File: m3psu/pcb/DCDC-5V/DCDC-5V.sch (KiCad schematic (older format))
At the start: 18 parts, among them J1 WEST TOP, J2 WEST BOT, J3 NORTH TOP, J4 EAST TOP, J5 EAST BOT, J6 NORTH BOT

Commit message: Work on DCDC-5V schematic and board
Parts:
- removed C?: 100n, symbol C
- added C1, C10, C6: 100n, agg:0402, symbol C
- added C11, C7: 3n3, agg:0402, symbol C
- added C12, C8, C9: 22µ, agg:0805, symbol C
- added C5: 10µ, agg:0805, symbol C
- added IC2: TPS62133, agg:QFN-16-EP-TI, symbol TPS62133
- added IC3: TPS62152, agg:QFN-16-EP-TI, symbol TPS62152
- added L1: 2µ2, agg:TYS5040, symbol L
- added L2: 3µ3, agg:VLS201610HBX-1, symbol L
- added Q1, Q2, Q3, Q4: NFET_GDS, agg:SOT-883-B, symbol NFET_GDS
- added Q5, Q6, Q7, Q8: PFET_GDS, agg:SON2x2, symbol PFET_GDS
- added R10, R11, R12, R13, R14, R15, R16, R9: 33k, agg:0402, symbol R
- added R17, R18, R19, R20: 10m, agg:0603, symbol R
- C2, C3, C4: renamed from C?; footprint (none) -> agg:0402
- R2, R3, R4, R5, R6, R7, R8: renamed from R?; footprint (none) -> agg:0402
- gave numbers to parts that had none: 1
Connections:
- net 3v3: now also IC1.10 (VPWR), C1.2, C12.1, IC3.14 (VOS), IC3.7 (FSW), L2.2
- net 5v_CAM: now also IC1.44 (I_SENSE_1-), R18.1
- net 5v_CAN: now also IC1.42 (I_SENSE_0-), R17.1
- net 5v_IMU: now also IC1.46 (I_SENSE_2-), R19.1
- net 5v_RADIO: now also IC1.48 (I_SENSE_3-), R20.1
- net GND: now also C1.1, C10.2, C11.2, C12.2, C5.2, C6.2, C7.2, C8.2, C9.2, IC2.15 (PGND), IC2.16 (PGND), IC2.5 (FB), IC2.6 (AGND), IC2.7 (FSW), IC2.8 (DEF), IC2.EP, IC3.15 (PGND), IC3.16 (PGND), IC3.5 (FB), IC3.6 (AGND), IC3.8 (DEF), IC3.EP, Q1.S, Q2.S, Q3.S, Q4.S
- net VCC: now also C10.1, C5.1, C6.1, C9.1, IC2.10 (AVIN), IC2.11 (PVIN), IC2.12 (PVIN), IC2.13 (EN), IC3.10 (AVIN), IC3.11 (PVIN), IC3.12 (PVIN), IC3.13 (EN)
- net ISNS0+: now reaches IC1.1 (V_SENSE_0+)
- net ISNS0+: now also IC1.41 (I_SENSE_0+), Q5.D, R17.2
- net VEN_0: now reaches IC1.3 (VOUT_EN0)
- net VEN_0: now also Q1.G, R9.2
- net VEN_1: now reaches IC1.4 (VOUT_EN1)
- net VEN_1: now also Q2.G, R10.2
- net ISNS1+: now reaches IC1.43 (I_SENSE_1+)
- net ISNS1+: now also IC1.63 (V_SENSE_1+), Q6.D, R18.2
- net ISNS2+: now reaches IC1.45 (I_SENSE_2+)
- net ISNS2+: now also IC1.61 (V_SENSE_2+), Q7.D, R19.2
- net ISNS3+: now reaches IC1.47 (I_SENSE_3+)
- net ISNS3+: now also IC1.49 (V_SENSE_3+), Q8.D, R20.2
- net VEN_2: now reaches IC1.5 (VOUT_EN2)
- net VEN_2: now also Q3.G, R11.2
- net V_DIST: now reaches IC1.55 (IIN_SENSE+)
- net V_DIST: now also IC1.56 (IIN_SENSE-), IC1.9 (VIN_SENSE), C8.1, IC2.14 (VOS), L1.2, Q5.S, Q6.S, Q7.S, Q8.S, R10.1, R11.1, R12.1, R13.1, R14.1, R15.1, R16.1, R9.1
- net VEN_3: now reaches IC1.6 (VOUT_EN3)
- net VEN_3: now also Q4.G, R12.2
- new net: IC2.1 (SW), IC2.2 (SW), IC2.3 (SW), L1.1
- new net: C7.1, IC2.9 (SS/TR)
- new net: IC3.1 (SW), IC3.2 (SW), IC3.3 (SW), L2.1
- new net: C11.1, IC3.9 (SS/TR)
- new net: Q1.D, Q5.G, R13.2
- new net: Q2.D, Q6.G, R14.2
- new net: Q3.D, Q7.G, R15.2
- new net: Q4.D, Q8.G, R16.2
- no-connect marks 13 -> 15
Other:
- note added: "3.3V 1A fixed output"
- note added: "5V 3A fixed output"
- note added: "CHANNEL 0"
- note added: "CHANNEL 1"
- note added: "CHANNEL 2"
- note added: "CHANNEL 3"
- moved on the sheet: C2

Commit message: Add note about temporary footprint
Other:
- note added: "WRONG FOOTPRINT\nTEMPORARILY"
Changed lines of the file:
@@
 Wire Wire Line
 	9800 4000 9800 3950
+Text Notes 2400 1100 0    60   ~ 0
+WRONG FOOTPRINT\nTEMPORARILY
 $EndSCHEMATC

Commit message: Finish DCDC-5V schematic, first go at routing
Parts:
- added R1: 5k49, agg:0402, symbol R
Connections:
- net 3v3: now also R1.1
- net GND: now also IC1.15 (TSENSE_0), IC1.16 (TSENSE_1), IC1.27 (TSENSE_2), IC1.34 (TSENSE_3)
- net PSU_RSVD: now reaches J3.5
- net PSU_RSVD: now also J6.5
- net at IC1.18 (SHARE_CLK): now also R1.2
- no-connect marks 15 -> 8

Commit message: Update with correct inductor footprint
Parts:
- L1: footprint agg:TYS5040 -> agg:XFL4020
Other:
- note removed: "WRONG FOOTPRINT\nTEMPORARILY"
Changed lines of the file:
@@
 F 0 "L1" H 2500 1250 50  0000 C CNN
 F 1 "2µ2" H 2500 1150 50  0000 C CNN
-F 2 "agg:TYS5040" H 2450 1200 50  0001 C CNN
+F 2 "agg:XFL4020" H 2450 1200 50  0001 C CNN
 F 3 "" H 2450 1200 50  0001 C CNN
 F 4 "2289216" H 2450 1200 60  0001 C CNN "Farnell"
@@
 	1    0    0    -1
 $EndComp
-Text Notes 2400 1100 0    60   ~ 0
-WRONG FOOTPRINT\nTEMPORARILY
 Text Label 10100 3500 2    60   ~ 0
 PSU_RSVD
@@
 	8750 700  8750 750
 $Comp
-L GND #PWR?
+L GND #PWR054
 U 1 1 58B616BB
 P 5300 4950
-F 0 "#PWR?" H 5170 4990 50  0001 L CNN
+F 0 "#PWR054" H 5170 4990 50  0001 L CNN
 F 1 "GND" H 5300 4850 50  0000 C CNN
 F 2 "" H 5300 4950 60  0001 C CNN
@@
 	5300 4950 5250 4950
 $Comp
-L GND #PWR?
+L GND #PWR055
 U 1 1 58B61DC1
 P 5300 4150
-F 0 "#PWR?" H 5170 4190 50  0001 L CNN
+F 0 "#PWR055" H 5170 4190 50  0001 L CNN
 F 1 "GND" H 5300 4050 50  0000 C CNN
 F 2 "" H 5300 4150 60  0001 C CNN
@@
 	5300 4150 5250 4150
 $Comp
-L GND #PWR?
+L GND #PWR056
 U 1 1 58B62495
 P 5300 3350
-F 0 "#PWR?" H 5170 3390 50  0001 L CNN
+F 0 "#PWR056" H 5170 3390 50  0001 L CNN
 F 1 "GND" H 5300 3250 50  0000 C CNN
 F 2 "" H 5300 3350 60  0001 C CNN
@@
 	5300 3350 5250 3350
 $Comp
-L GND #PWR?
+L GND #PWR057
 U 1 1 58B62E35
 P 5300 2550
-F 0 "#PWR?" H 5170 2590 50  0001 L CNN
+F 0 "#PWR057" H 5170 2590 50  0001 L CNN
 F 1 "GND" H 5300 2450 50  0000 C CNN
 F 2 "" H 5300 2550 60  0001 C CNN

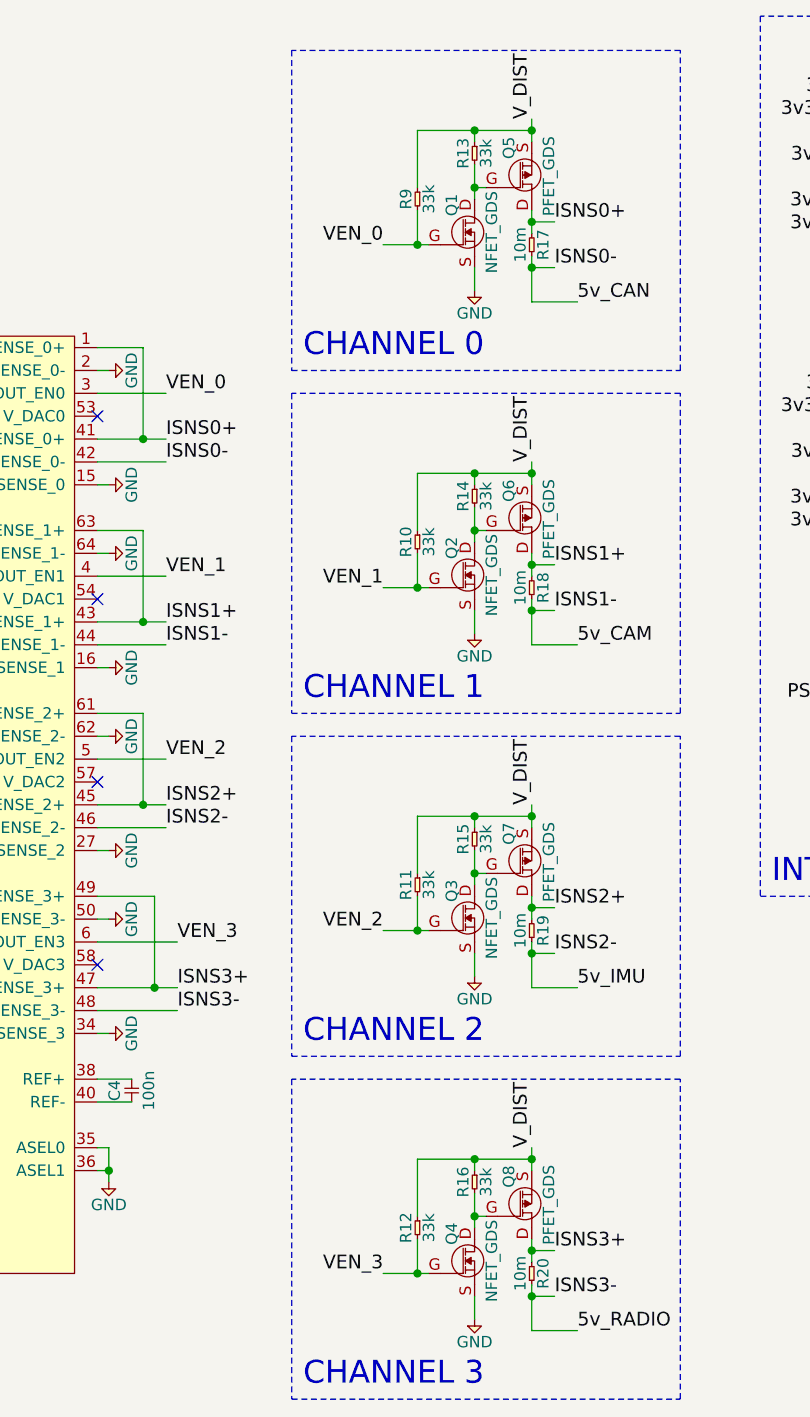
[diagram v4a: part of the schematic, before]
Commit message: Update NFET footprint on 5v board, add pull-downs
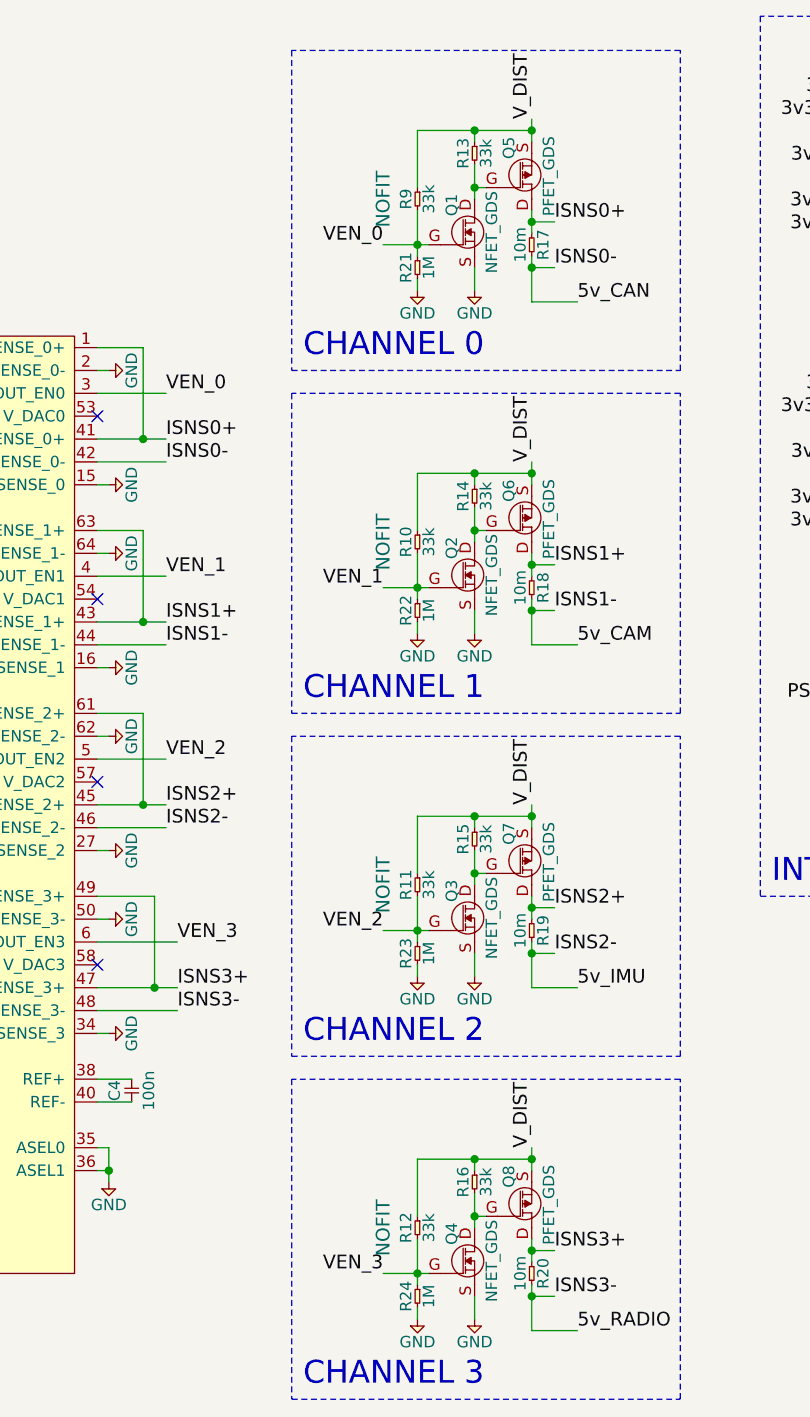
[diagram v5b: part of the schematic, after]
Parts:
- added R21, R22, R23, R24: 1M, agg:0402, symbol R
- Q1, Q2, Q3, Q4: footprint agg:SOT-883-B -> agg:PowerPAK-SC-75-6L-Single; Farnell (none) -> 2364070
- R10, R11, R12, R9: Fit (none) -> NOFIT
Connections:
- net GND: now also R21.2, R22.2, R23.2, R24.2
- net VEN_0: now also R21.1
- net VEN_1: now also R22.1
- net VEN_2: now also R23.1
- net VEN_3: now also R24.1
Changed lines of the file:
@@
 F 2 "agg:0402" H 6650 1250 50  0001 C CNN
 F 3 "" H 6650 1250 50  0001 C CNN
+F 4 "NOFIT" H 6700 1100 60  0000 C CNN "Fit"
 	1    6650 1250
 	0    1    1    0
@@
 F 2 "agg:0402" H 6650 2750 50  0001 C CNN
 F 3 "" H 6650 2750 50  0001 C CNN
+F 4 "NOFIT" H 6700 2600 60  0000 C CNN "Fit"
 	1    6650 2750
 	0    1    1    0
@@
 F 2 "agg:0402" H 6650 4250 50  0001 C CNN
 F 3 "" H 6650 4250 50  0001 C CNN
+F 4 "NOFIT" H 6700 4100 60  0000 C CNN "Fit"
 	1    6650 4250
 	0    1    1    0
@@
 F 2 "agg:0402" H 6650 5750 50  0001 C CNN
 F 3 "" H 6650 5750 50  0001 C CNN
+F 4 "NOFIT" H 6700 5600 60  0000 C CNN "Fit"
 	1    6650 5750
 	0    1    1    0
@@
 F 0 "Q1" V 6800 1425 50  0000 L CNN
 F 1 "NFET_GDS" V 6975 1175 50  0000 L CNN
-F 2 "agg:SOT-883-B" H 6900 1400 50  0001 C CNN
-F 3 "" H 6900 1400 50  0001 C CNN
+F 2 "agg:PowerPAK-SC-75-6L-Single" H 6900 1400 50  0001 C CNN
+F 3 "http://www.farnell.com/datasheets/2049550.pdf" H 6900 1400 50  0001 C CNN
+F 4 "2364070" V 6900 1400 60  0001 C CNN "Farnell"
 	1    6900 1400
-	1    0    0    -1
-$EndComp
-$Comp
-L NFET_GDS Q2
-U 1 1 58B86D5D
-P 6900 2900
-F 0 "Q2" V 6800 2925 50  0000 L CNN
-F 1 "NFET_GDS" V 6975 2675 50  0000 L CNN
-F 2 "agg:SOT-883-B" H 6900 2900 50  0001 C CNN
-F 3 "" H 6900 2900 50  0001 C CNN
-	1    6900 2900
-	1    0    0    -1
-$EndComp
-$Comp
-L NFET_GDS Q3
-U 1 1 58B86E0A
-P 6900 4400
-F 0 "Q3" V 6800 4425 50  0000 L CNN
-F 1 "NFET_GDS" V 6975 4175 50  0000 L CNN
-F 2 "agg:SOT-883-B" H 6900 4400 50  0001 C CNN
-F 3 "" H 6900 4400 50  0001 C CNN
-	1    6900 4400
-	1    0    0    -1
-$EndComp
-$Comp
-L NFET_GDS Q4
-U 1 1 58B86EE2
-P 6900 5900
-F 0 "Q4" V 6800 5925 50  0000 L CNN
-F 1 "NFET_GDS" V 6975 5675 50  0000 L CNN
-F 2 "agg:SOT-883-B" H 6900 5900 50  0001 C CNN
-F 3 "" H 6900 5900 50  0001 C CNN
-	1    6900 5900
 	1    0    0    -1
 $EndComp
@@
 Connection ~ 6650 6000
 Wire Wire Line
-	6650 5850 6650 6000
+	6650 5850 6650 6050
 Connection ~ 6900 5500
 Wire Wire Line
@@
 Connection ~ 6650 4500
 Wire Wire Line
-	6650 4350 6650 4500
+	6650 4350 6650 4550
 Connection ~ 6900 4000
 Wire Wire Line
@@
 Connection ~ 6650 3000
 Wire Wire Line
-	6650 2850 6650 3000
+	6650 2850 6650 3050
 Connection ~ 6900 2500
 Wire Wire Line
@@
 Connection ~ 6650 1500
 Wire Wire Line
-	6650 1350 6650 1500
+	6650 1350 6650 1550
 Connection ~ 6900 1000
 Wire Wire Line
@@
 Wire Wire Line
 	5300 2550 5250 2550
+$Comp
+L R R21
+U 1 1 5973E367
+P 6650 1550
+F 0 "R21" H 6700 1500 50  0000 C CNN
+F 1 "1M" H 6700 1600 50  0000 C CNN
+F 2 "agg:0402" H 6650 1550 50  0001 C CNN
+F 3 "" H 6650 1550 50  0001 C CNN
+	1    6650 1550
+	0    1    1    0
+$EndComp
+$Comp
+L GND #PWR058
+U 1 1 5973E42D
+P 6650 1700
+F 0 "#PWR058" H 6520 1740 50  0001 L CNN
+F 1 "GND" H 6650 1600 50  0000 C CNN
+F 2 "" H 6650 1700 60  0001 C CNN
+F 3 "" H 6650 1700 60  0001 C CNN
+	1    6650 1700
+	1    0    0    -1
+$EndComp
+Wire Wire Line
+	6650 1700 6650 1650
+$Comp
+L R R22
+U 1 1 5973FD31
+P 6650 3050
+F 0 "R22" H 6700 3000 50  0000 C CNN
+F 1 "1M" H 6700 3100 50  0000 C CNN
+F 2 "agg:0402" H 6650 3050 50  0001 C CNN
+F 3 "" H 6650 3050 50  0001 C CNN
+	1    6650 3050
+	0    1    1    0
+$EndComp
+$Comp
+L GND #PWR059
+U 1 1 5973FD38
+P 6650 3200
+F 0 "#PWR059" H 6520 3240 50  0001 L CNN
+F 1 "GND" H 6650 3100 50  0000 C CNN
+F 2 "" H 6650 3200 60  0001 C CNN
+F 3 "" H 6650 3200 60  0001 C CNN
+	1    6650 3200
+	1    0    0    -1
+$EndComp
+Wire Wire Line
+	6650 3200 6650 3150
+$Comp
+L R R23
+U 1 1 59741207
+P 6650 4550
+F 0 "R23" H 6700 4500 50  0000 C CNN
+F 1 "1M" H 6700 4600 50  0000 C CNN
+F 2 "agg:0402" H 6650 4550 50  0001 C CNN
+F 3 "" H 6650 4550 50  0001 C CNN
+	1    6650 4550
+	0    1    1    0
+$EndComp
+$Comp
+L GND #PWR060
+U 1 1 5974120E
+P 6650 4700
+F 0 "#PWR060" H 6520 4740 50  0001 L CNN
+F 1 "GND" H 6650 4600 50  0000 C CNN
+F 2 "" H 6650 4700 60  0001 C CNN
+F 3 "" H 6650 4700 60  0001 C CNN
+	1    6650 4700
+	1    0    0    -1
+$EndComp
+Wire Wire Line
+	6650 4700 6650 4650
+$Comp
+L R R24
+U 1 1 59742152
+P 6650 6050
+F 0 "R24" H 6700 6000 50  0000 C CNN
+F 1 "1M" H 6700 6100 50  0000 C CNN
+F 2 "agg:0402" H 6650 6050 50  0001 C CNN
+F 3 "" H 6650 6050 50  0001 C CNN
+	1    6650 6050
+	0    1    1    0
+$EndComp
+$Comp
+L GND #PWR061
+U 1 1 59742159
+P 6650 6200
+F 0 "#PWR061" H 6520 6240 50  0001 L CNN
+F 1 "GND" H 6650 6100 50  0000 C CNN
+F 2 "" H 6650 6200 60  0001 C CNN
+F 3 "" H 6650 6200 60  0001 C CNN
+	1    6650 6200
+	1    0    0    -1
+$EndComp
+Wire Wire Line
+	6650 6200 6650 6150
+$Comp
+L NFET_GDS Q2
+U 1 1 5974C679
+P 6900 2900
+F 0 "Q2" V 6800 2925 50  0000 L CNN
+F 1 "NFET_GDS" V 6975 2675 50  0000 L CNN
+F 2 "agg:PowerPAK-SC-75-6L-Single" H 6900 2900 50  0001 C CNN
+F 3 "http://www.farnell.com/datasheets/2049550.pdf" H 6900 2900 50  0001 C CNN
+F 4 "2364070" V 6900 2900 60  0001 C CNN "Farnell"
+	1    6900 2900
+	1    0    0    -1
+$EndComp
+$Comp
+L NFET_GDS Q3
+U 1 1 5974C74A
+P 6900 4400
+F 0 "Q3" V 6800 4425 50  0000 L CNN
+F 1 "NFET_GDS" V 6975 4175 50  0000 L CNN
+F 2 "agg:PowerPAK-SC-75-6L-Single" H 6900 4400 50  0001 C CNN
+F 3 "http://www.farnell.com/datasheets/2049550.pdf" H 6900 4400 50  0001 C CNN
+F 4 "2364070" V 6900 4400 60  0001 C CNN "Farnell"
+	1    6900 4400
+	1    0    0    -1
+$EndComp
+$Comp
+L NFET_GDS Q4
+U 1 1 5974CAF6
+P 6900 5900
+F 0 "Q4" V 6800 5925 50  0000 L CNN
+F 1 "NFET_GDS" V 6975 5675 50  0000 L CNN
+F 2 "agg:PowerPAK-SC-75-6L-Single" H 6900 5900 50  0001 C CNN
+F 3 "http://www.farnell.com/datasheets/2049550.pdf" H 6900 5900 50  0001 C CNN
+F 4 "2364070" V 6900 5900 60  0001 C CNN "Farnell"
+	1    6900 5900
+	1    0    0    -1
+$EndComp
 $EndSCHEMATC

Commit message: Fix silkscreen, add test pads
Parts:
- added TP1, TP2, TP3, TP4: TESTPAD, agg:TESTPAD, symbol TESTPAD
- C12, C8, C9: value 22µ -> 22u
- C5: value 10µ -> 10u
- J3: Samtec (none) -> TFML-105-02-L-D
- J6: Samtec (none) -> SFML-105-02-L-D-LC
- L1: value 2µ2 -> 2u2
- L2: value 3µ3 -> 3u3
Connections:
- net GND: now also TP4.1 (TP)
- net SCL: now also TP2.1 (TP)
- net SDA: now also TP1.1 (TP)
- net ~ALERT: now also TP3.1 (TP)
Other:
- note added: "TEST POINTS"

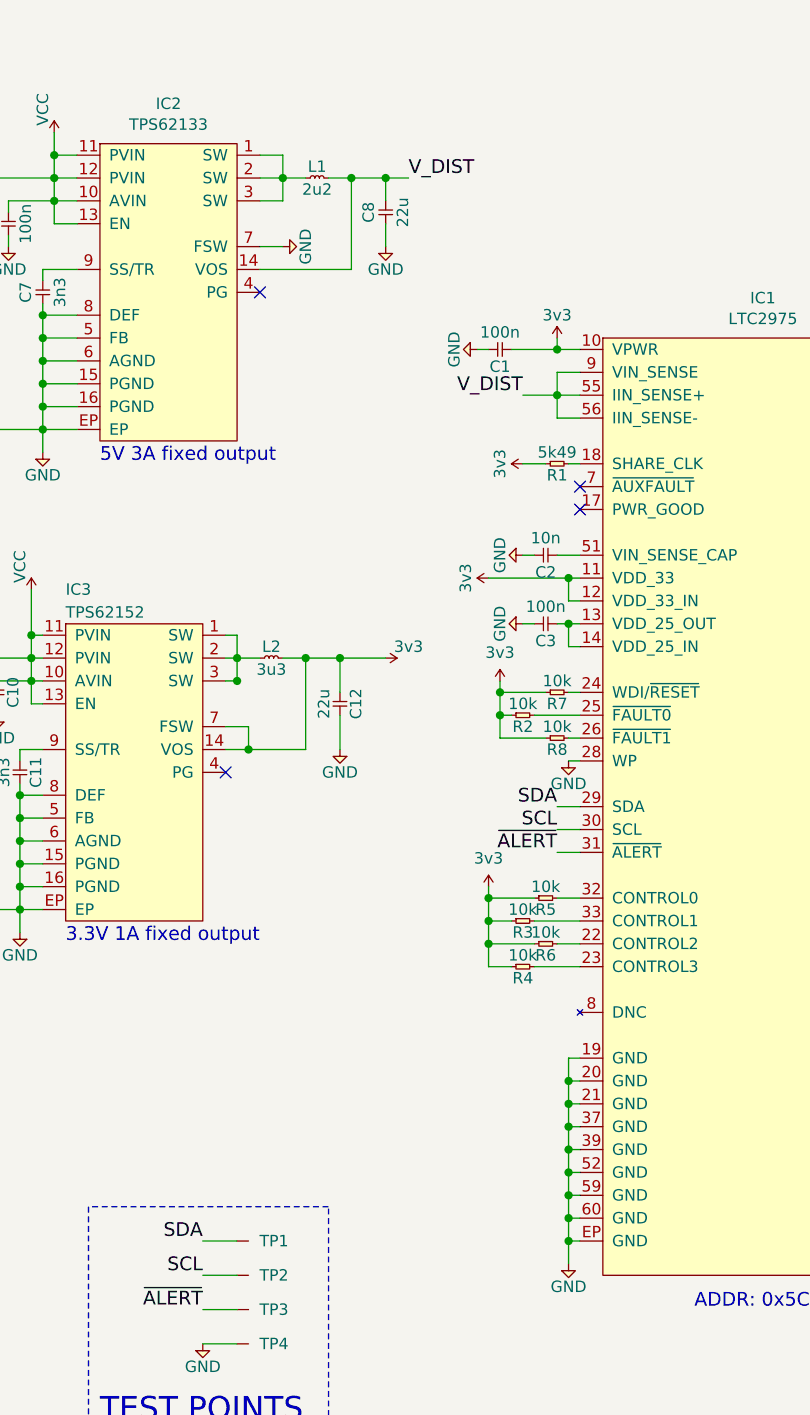
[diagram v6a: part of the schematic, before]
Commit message: Add additional decoupling capacitor to 5V board
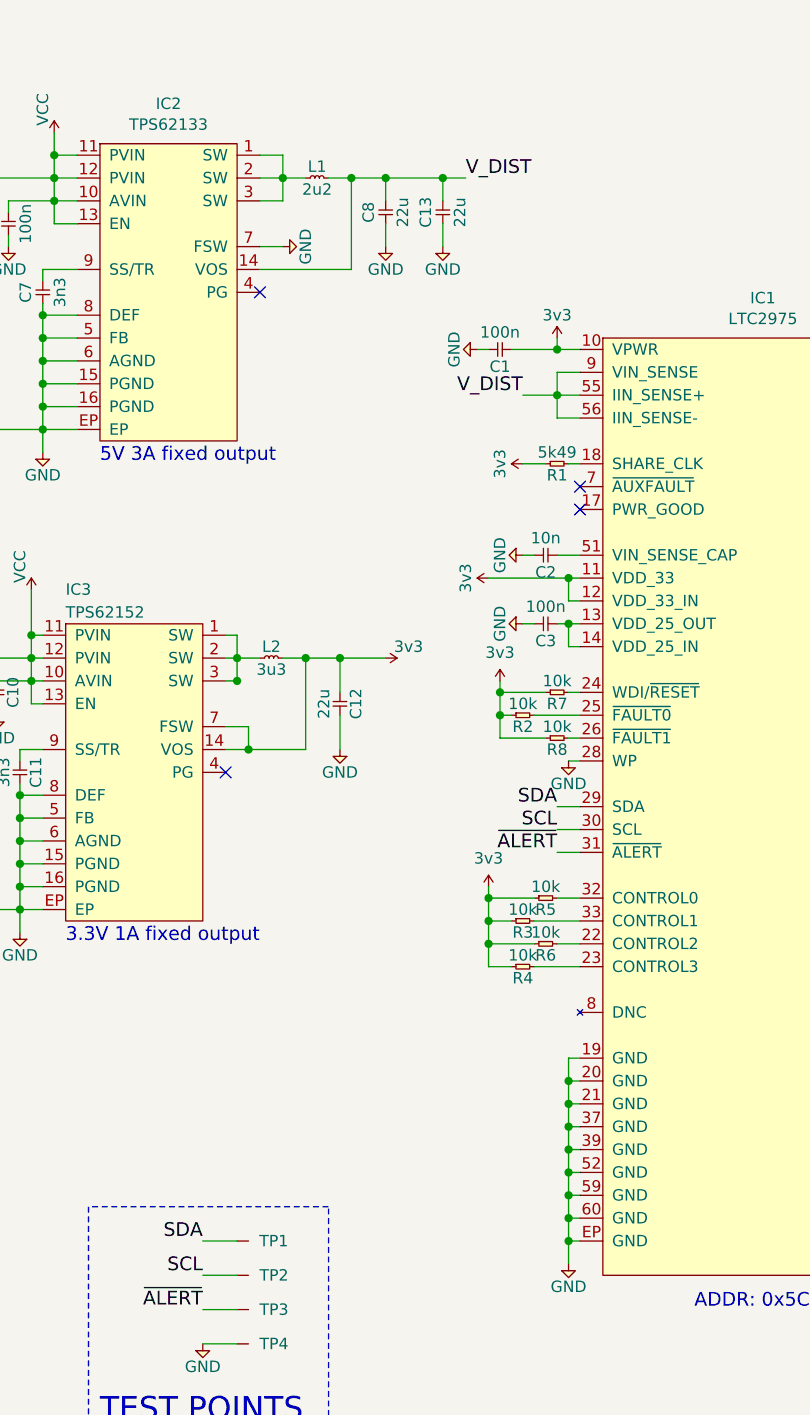
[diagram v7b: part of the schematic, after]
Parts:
- added C13: 22u, agg:0805, symbol C
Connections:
- net GND: now also C13.2
- net V_DIST: now also C13.1
